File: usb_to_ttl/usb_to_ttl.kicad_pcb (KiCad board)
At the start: 2 copper layers, 15 parts, among them J1 Debug, P1 USB_C_Plug_USB2.0, P2 USB_C_Plug_USB2.0, U1 CP2102N-Axx-xQFN28, U2 TLV1117-33

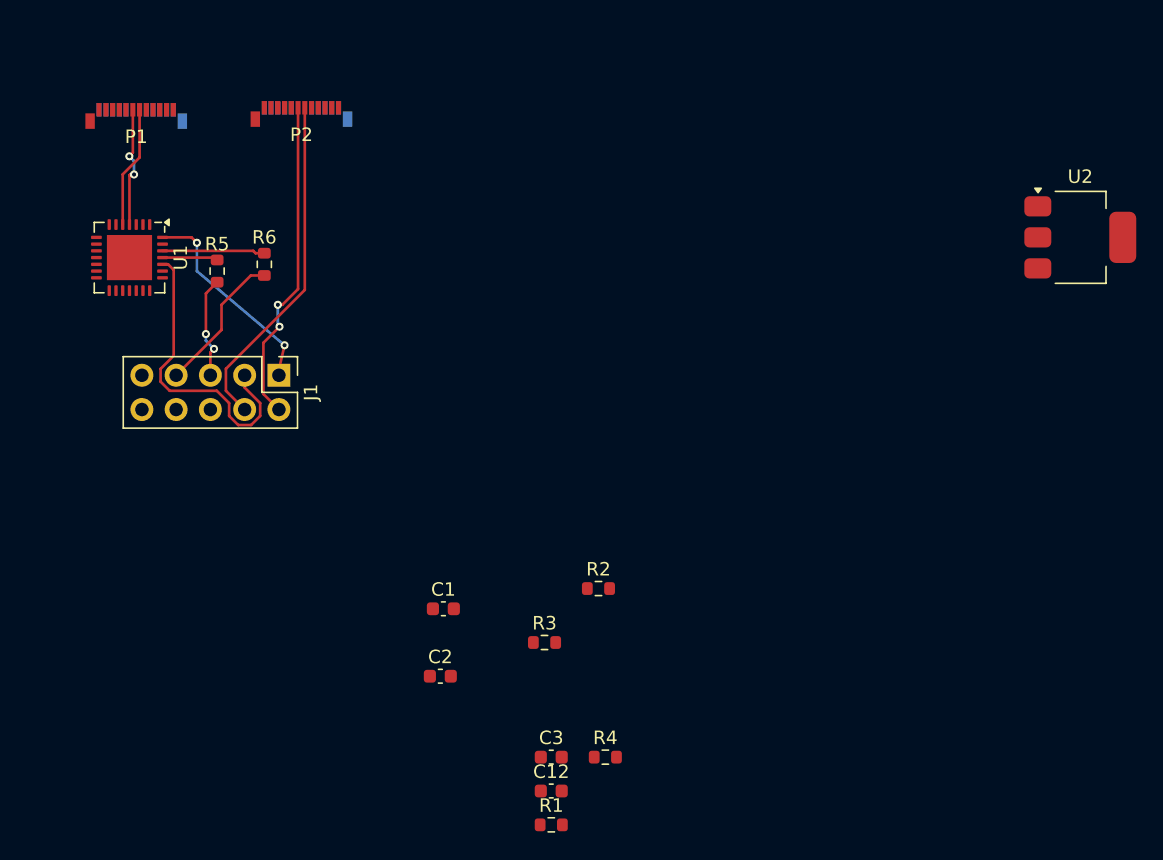
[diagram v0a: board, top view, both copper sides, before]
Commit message: Updated adapter/debugger schematic and PCB files
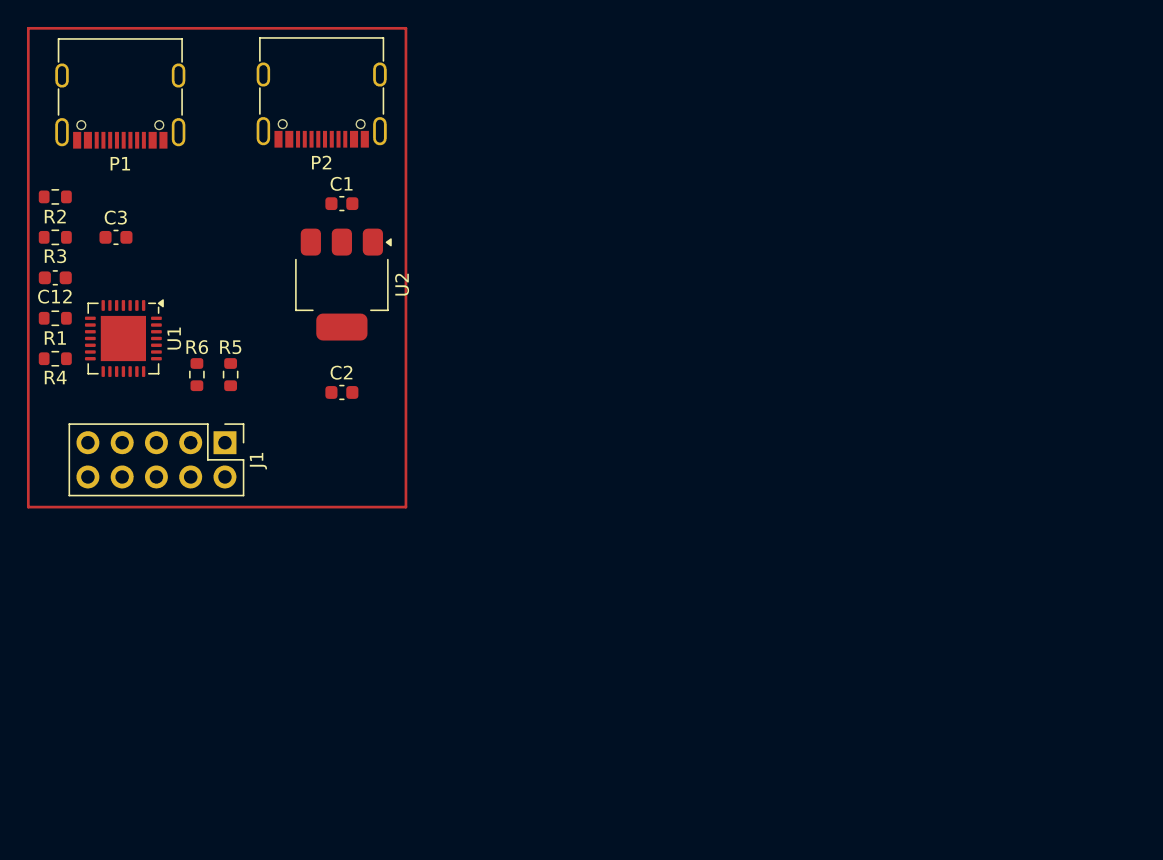
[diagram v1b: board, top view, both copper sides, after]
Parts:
- P1, P2: footprint Connector_USB:USB_C_Plug_Molex_105444 -> Connector_USB:USB_C_Receptacle_G-Switch_GT-USB-7010ASV
- moved U2 54.9 mm to (37.2, 30.0), turned to -90 degrees
- moved C12 52.9 mm to (16.0, 29.5), turned to 180 degrees
- moved R1 52.6 mm to (16.0, 32.5)
- moved R4 50.4 mm to (16.0, 35.5), turned to 180 degrees
- moved C3 50.3 mm to (20.5, 26.5)
- moved R2 49.7 mm to (16.0, 23.5)
- moved R3 47.1 mm to (16.0, 26.5), turned to 180 degrees
- moved C1 31.0 mm to (37.2, 24.0)
- moved C2 22.3 mm to (37.2, 38.0)
- moved R6 9.58 mm to (26.5, 36.7)
- moved R5 7.74 mm to (29.0, 36.7)
- moved J1 6.40 mm to (28.6, 41.7)
- moved U1 6.02 mm to (21.1, 34.0)
- moved P2 2.02 mm to (35.8, 15.5), turned to 180 degrees
- moved P1 1.85 mm to (20.8, 15.6), turned to 180 degrees
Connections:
- J1 pad 2: /USB_D+ -> /USB2_D+
- J1 pad 4: /USB_D- -> /USB2_D-
- P1 pad A6: /USB_D+ -> /USB1_D+
- P1 pad A7: /USB_D- -> /USB1_D-
- P1 pad S1: unconnected-(P1-SHIELD-PadS1)_1 -> GND
- P2 pad A6: /USB_D+ -> /USB2_D+
- P2 pad A7: /USB_D- -> /USB2_D-
- P2 pad S1: unconnected-(P2-SHIELD-PadS1)_1 -> GND
- U1 pad 4: /USB_D+ -> /USB1_D+
- U1 pad 5: /USB_D- -> /USB1_D-
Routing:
- net /USB_D-: track 34.4 -> 0.00 mm
- net /USB_D+: track 33.3 -> 0.00 mm, vias 4 -> 0
- net /RTS: track 22.7 -> 0.00 mm
- net /DTR: track 15.6 -> 0.00 mm, vias 2 -> 0
- net /RX: track 10.7 -> 0.00 mm
- net Net-(U1-TXD): track 7.62 -> 0.00 mm
- net /TX: track 7.60 -> 0.00 mm, vias 2 -> 0
- net Net-(U1-RXD): track 4.12 -> 0.00 mm

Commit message: USB to TTL Adapter design complete
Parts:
- C2: footprint Capacitor_SMD:C_0603_1608Metric -> Capacitor_SMD:C_0805_2012Metric
- moved R1 1.12 mm to (15.5, 33.5)
- moved R4 1.12 mm to (15.5, 36.5)
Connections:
- J1 pad 5: /TX -> /RX
- J1 pad 7: /RX -> /TX
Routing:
- net +3V3: track 0.00 -> 44.7 mm
- net +5V: track 0.00 -> 44.4 mm
- net /USB2_D-: track 0.00 -> 31.8 mm, vias 0 -> 2
- net /USB2_D+: track 0.00 -> 31.6 mm, vias 0 -> 2
- net /DTR: track 0.00 -> 14.7 mm
- net /RTS: track 0.00 -> 14.3 mm
- net /USB1_D+: track 0.00 -> 12.7 mm, vias 0 -> 2
- net /USB1_D-: track 0.00 -> 12.4 mm, vias 0 -> 2
- net Net-(U1-VBUS): track 0.00 -> 10.1 mm, vias 0 -> 2
- net /TX: track 0.00 -> 8.13 mm
- net /RX: track 0.00 -> 7.29 mm
- net GND: track 0.00 -> 6.88 mm, vias 0 -> 5
- net Net-(U1-RXD): track 0.00 -> 6.27 mm
- net Net-(U1-TXD): track 0.00 -> 5.46 mm, vias 0 -> 2
- net Net-(U1-SUSPEND): track 0.00 -> 3.85 mm
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- added copper zone on B.Cu, net GND
- added copper zone on F.Cu, net GND
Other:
- board outline added: 31 x 37.5 mm
- board text added: "${TITLE} ${ISSUE_DATE} ${REVISION} ${COMPANY}"

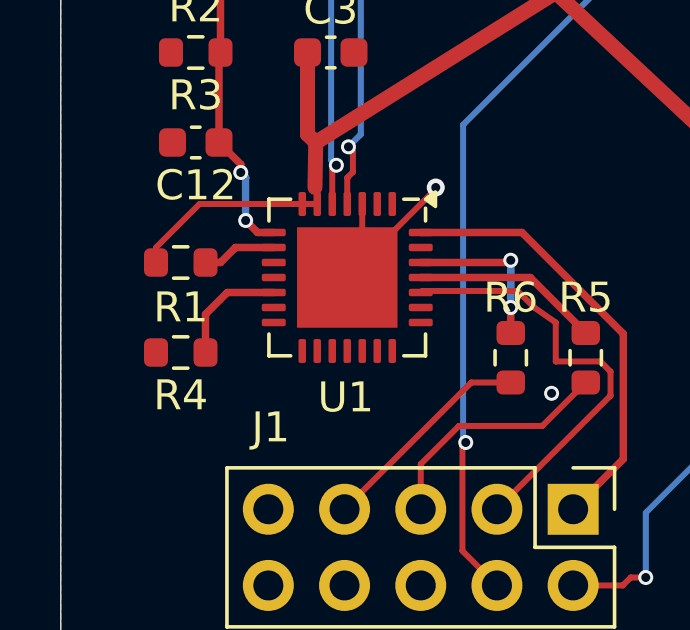
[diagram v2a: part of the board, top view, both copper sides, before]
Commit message: Fixed connection to SUSPEND pins
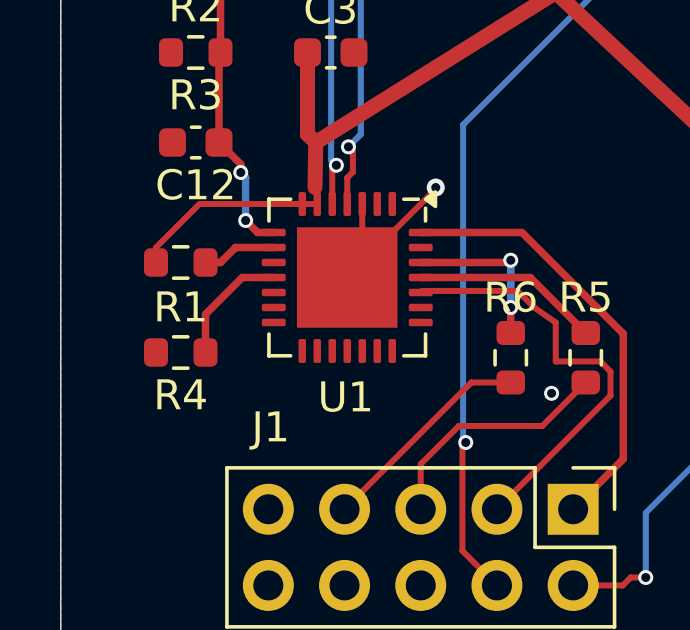
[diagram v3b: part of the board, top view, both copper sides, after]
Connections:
- R4 pad 1: Net-(U1-SUSPEND) -> Net-(U1-~{SUSPEND})
- U1 pad 11: unconnected-(U1-~{SUSPEND}-Pad11) -> Net-(U1-~{SUSPEND})
- U1 pad 12: Net-(U1-SUSPEND) -> unconnected-(U1-SUSPEND-Pad12)
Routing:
- net Net-(U1-~{SUSPEND}): track 0.00 -> 4.06 mm
- net Net-(U1-SUSPEND): track 3.85 -> 0.00 mm
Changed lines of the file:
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@@
 	(net 8 "/RTS")
 	(net 9 "Net-(U1-~{RST})")
-	(net 10 "Net-(U1-SUSPEND)")
+	(net 10 "Net-(U1-~{SUSPEND})")
 	(net 11 "Net-(U1-TXD)")
 	(net 12 "unconnected-(U1-~{RI}{slash}CLK-Pad2)")
-	(net 13 "unconnected-(U1-~{SUSPEND}-Pad11)")
+	(net 13 "unconnected-(U1-SUSPEND-Pad12)")
 	(net 14 "unconnected-(U1-GPIO.5-Pad21)")
 	(net 15 "unconnected-(U1-~{DSR}-Pad27)")
@@
 			(layers "F.Cu" "F.Mask" "F.Paste")
 			(roundrect_rratio 0.25)
-			(net 10 "Net-(U1-SUSPEND)")
+			(net 10 "Net-(U1-~{SUSPEND})")
 			(pintype "passive")
 		)
@@
 			(layers "F.Cu" "F.Mask" "F.Paste")
 			(roundrect_rratio 0.25)
-			(net 13 "unconnected-(U1-~{SUSPEND}-Pad11)")
+			(net 10 "Net-(U1-~{SUSPEND})")
 			(pinfunction "~{SUSPEND}")
-			(pintype "output+no_connect")
+			(pintype "output")
 		)
 		(pad "12" smd roundrect
@@
 			(layers "F.Cu" "F.Mask" "F.Paste")
 			(roundrect_rratio 0.25)
-			(net 10 "Net-(U1-SUSPEND)")
+			(net 13 "unconnected-(U1-SUSPEND-Pad12)")
 			(pinfunction "SUSPEND")
-			(pintype "output")
+			(pintype "output+no_connect")
 		)
 		(pad "13" smd roundrect
@@
 	)
 	(segment
-		(start 18.6 34.5)
-		(end 17.049418 34.5)
+		(start 16.325 36.5)
+		(end 16.325 35.224418)
 		(width 0.25)
 		(layer "F.Cu")
@@
 	)
 	(segment
-		(start 16.325 35.224418)
-		(end 16.325 36.5)
+		(start 17.549418 34)
+		(end 18.6 34)
 		(width 0.25)
 		(layer "F.Cu")
@@
 	)
 	(segment
-		(start 17.049418 34.5)
-		(end 16.325 35.224418)
+		(start 16.325 35.224418)
+		(end 17.549418 34)
 		(width 0.25)
 		(layer "F.Cu")

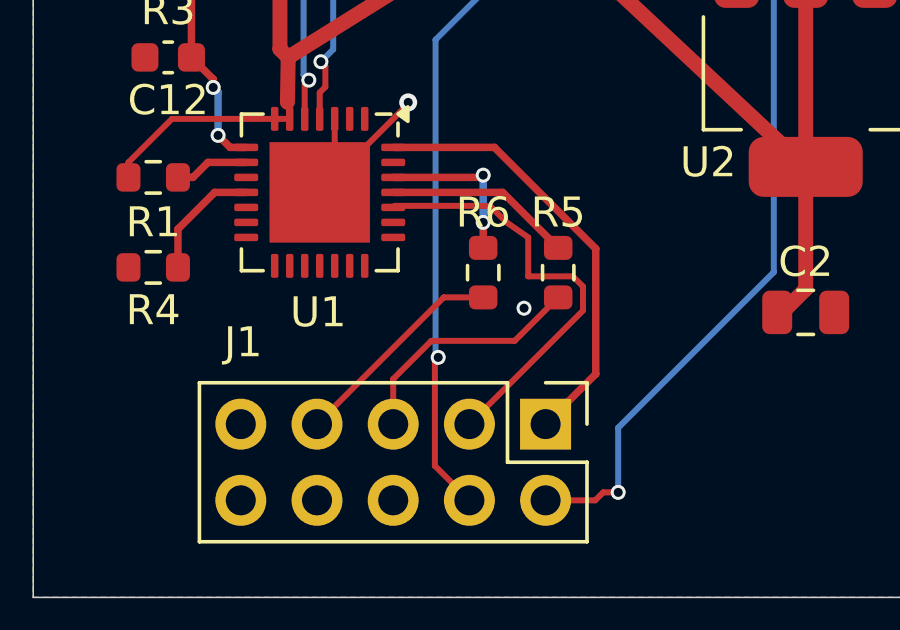
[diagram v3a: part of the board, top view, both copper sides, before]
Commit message: Fixed TX/RX connection on the board
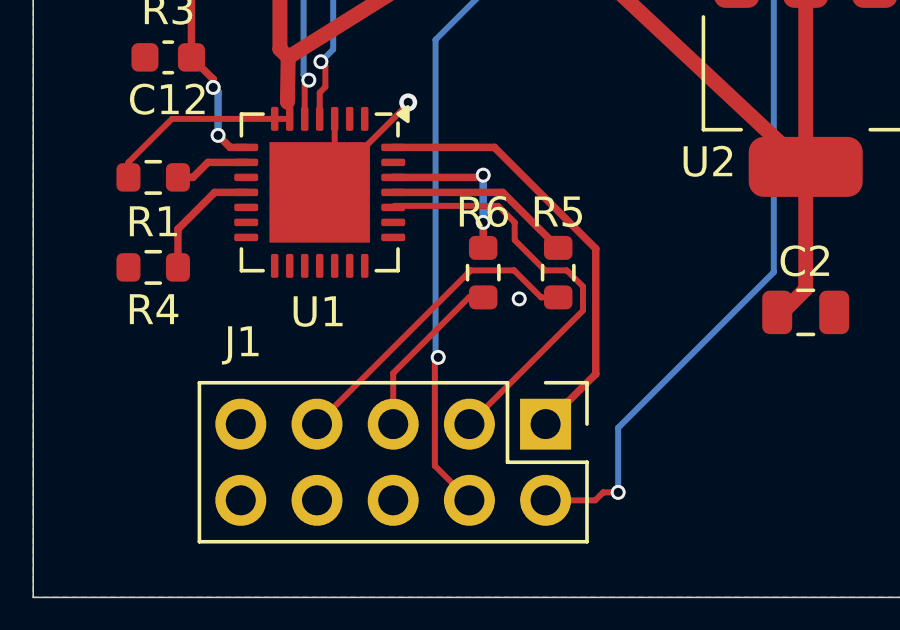
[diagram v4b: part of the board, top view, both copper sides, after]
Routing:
- net /TX: track 8.13 -> 10.5 mm
- net /RX: track 7.29 -> 5.75 mm
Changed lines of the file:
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@@
 	)
 	(via
-		(at 27.861091 37.861091)
+		(at 27.7 37.55)
 		(size 0.5)
 		(drill 0.3)
@@
 	)
 	(segment
-		(start 25.185 37.5)
-		(end 20.96 41.725)
+		(start 26.5 37.5)
+		(end 26.025 37.5)
 		(width 0.2)
 		(layer "F.Cu")
@@
 	)
 	(segment
-		(start 26.5 37.5)
-		(end 25.185 37.5)
+		(start 23.5 40.025)
+		(end 23.5 41.725)
+		(width 0.2)
+		(layer "F.Cu")
+		(net 5)
+	)
+	(segment
+		(start 26.025 37.5)
+		(end 23.5 40.025)
 		(width 0.2)
 		(layer "F.Cu")
@@
 	)
 	(segment
+		(start 26.085 36.6)
+		(end 20.96 41.725)
+		(width 0.2)
+		(layer "F.Cu")
+		(net 7)
+	)
+	(segment
 		(start 29 37.5)
-		(end 27.551 38.949)
+		(end 28.429232 37.5)
 		(width 0.2)
 		(layer "F.Cu")
@@
 	)
 	(segment
-		(start 27.551 38.949)
-		(end 24.771768 38.949)
+		(start 28.429232 37.5)
+		(end 27.529232 36.6)
 		(width 0.2)
 		(layer "F.Cu")
@@
 	)
 	(segment
-		(start 24.771768 38.949)
-		(end 23.5 40.220768)
+		(start 27.529232 36.6)
+		(end 26.085 36.6)
 		(width 0.2)
 		(layer "F.Cu")
 		(net 7)
-	)
-	(segment
-		(start 23.5 40.220768)
-		(end 23.5 41.725)
-		(width 0.2)
-		(layer "F.Cu")
-		(net 7)
-	)
-	(segment
-		(start 28 35.5)
-		(end 28 36.799)
-		(width 0.2)
-		(layer "F.Cu")
-		(net 8)
-	)
-	(segment
-		(start 27.276 34.996768)
-		(end 28 35.5)
-		(width 0.2)
-		(layer "F.Cu")
-		(net 8)
-	)
-	(segment
-		(start 29.488064 36.799)
-		(end 29.826 37.136936)
-		(width 0.2)
-		(layer "F.Cu")
-		(net 8)
 	)
 	(segment
@@
 	)
 	(segment
+		(start 29.289064 36.6)
+		(end 29.826 37.136936)
+		(width 0.2)
+		(layer "F.Cu")
+		(net 8)
+	)
+	(segment
+		(start 28.560936 36.6)
+		(end 29.289064 36.6)
+		(width 0.2)
+		(layer "F.Cu")
+		(net 8)
+	)
+	(segment
 		(start 23.551 34.449)
-		(end 26.728232 34.449)
-		(width 0.2)
-		(layer "F.Cu")
-		(net 8)
-	)
-	(segment
-		(start 26.728232 34.449)
-		(end 27.276 34.996768)
-		(width 0.2)
-		(layer "F.Cu")
-		(net 8)
-	)
-	(segment
-		(start 28 36.799)
-		(end 29.488064 36.799)
+		(end 26.996546 34.449)
+		(width 0.2)
+		(layer "F.Cu")
+		(net 8)
+	)
+	(segment
+		(start 26.996546 34.449)
+		(end 27.55 35.002454)
+		(width 0.2)
+		(layer "F.Cu")
+		(net 8)
+	)
+	(segment
+		(start 27.55 35.002454)
+		(end 27.55 35.589064)
 		(width 0.2)
 		(layer "F.Cu")
@@
 		(width 0.2)
 		(layer "F.Cu")
+		(net 8)
+	)
+	(segment
+		(start 27.55 35.589064)
+		(end 28.560936 36.6)
+		(width 0.2)
+		(layer "F.Cu")

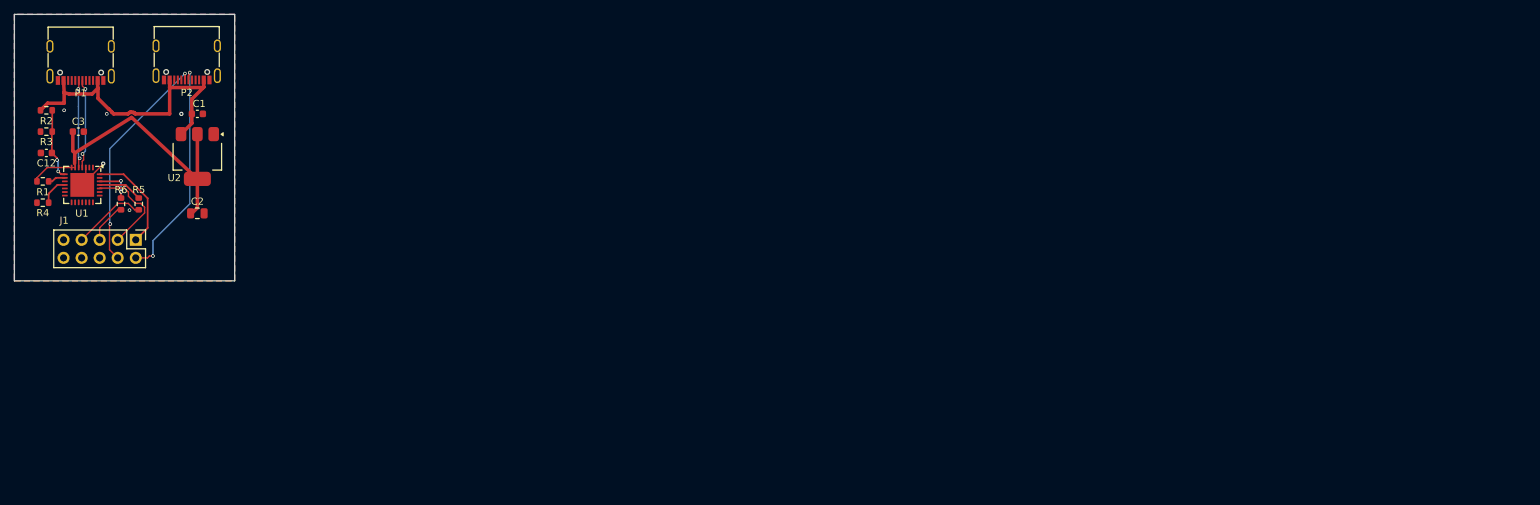
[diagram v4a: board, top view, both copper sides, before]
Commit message: Added mounting holes
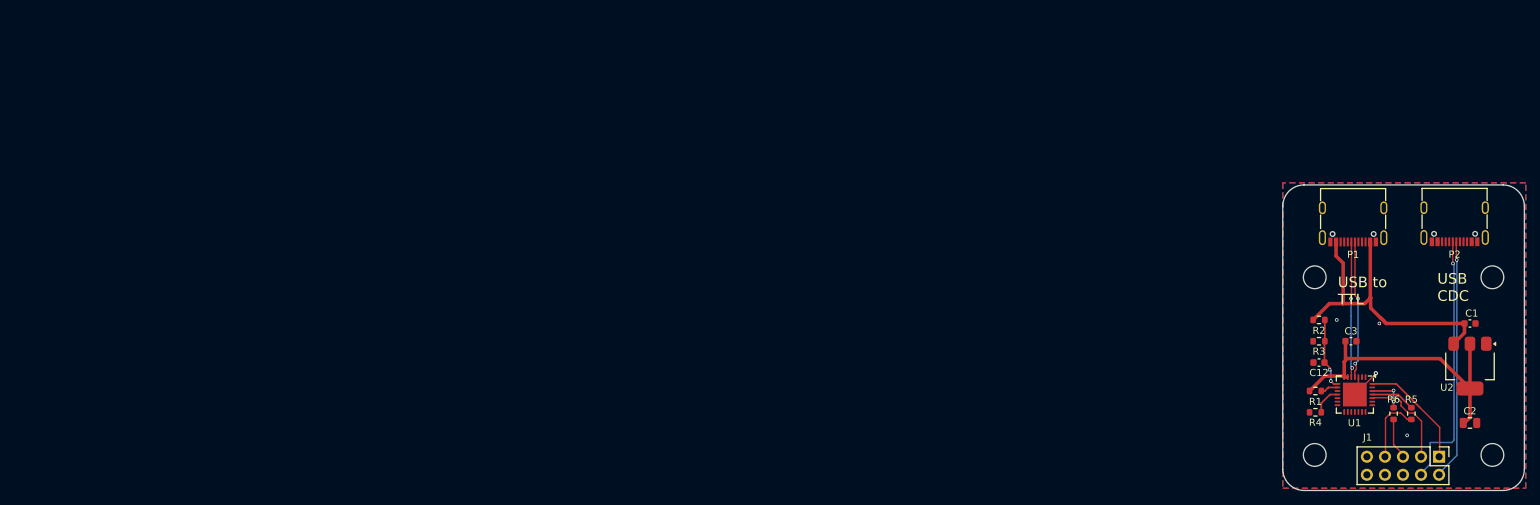
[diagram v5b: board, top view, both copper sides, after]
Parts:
- added H1: MountingHole, MountingHole:MountingHole_3.2mm_M3_ISO7380, F.Cu at (194.5, 47.0)
- added H2: MountingHole, MountingHole:MountingHole_3.2mm_M3_ISO7380, F.Cu at (219.5, 47.0)
- added H3: MountingHole, MountingHole:MountingHole_3.2mm_M3_ISO7380, F.Cu at (194.5, 72.0)
- added H4: MountingHole, MountingHole:MountingHole_3.2mm_M3_ISO7380, F.Cu at (219.5, 72.0)
- moved J1 185.9 mm to (212.0, 72.2)
- moved C1 181.5 mm to (216.3, 53.5)
- moved C12 181.5 mm to (195.1, 59.0)
- moved C2 181.5 mm to (216.3, 67.5)
- moved C3 181.5 mm to (199.6, 56.0)
- moved R1 181.5 mm to (194.6, 63.0)
- moved R2 181.5 mm to (195.1, 53.0)
- moved R3 181.5 mm to (195.1, 56.0)
- moved R4 181.5 mm to (194.6, 66.0)
- moved R5 181.5 mm to (208.1, 66.2)
- moved R6 181.5 mm to (205.6, 66.2)
- moved U2 181.5 mm to (216.3, 59.5)
- moved U1 181.5 mm to (200.1, 63.5)
- moved P1 180.5 mm to (199.9, 38.3)
- moved P2 179.9 mm to (214.2, 38.3)
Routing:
- net /USB1_D+: track 12.7 -> 19.5 mm
- net /USB1_D-: track 12.4 -> 19.2 mm
- net /USB2_D-: track 31.8 -> 36.6 mm, vias 2 -> 1
- net +3V3: track 44.7 -> 41.8 mm
- net /USB2_D+: track 31.6 -> 33.9 mm, vias 2 -> 1
- net /DTR: track 14.7 -> 16.2 mm
- net +5V: track 44.4 -> 45.5 mm
- net /TX: track 10.5 -> 9.77 mm
- net GND: vias 5 -> 4
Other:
- board size 31 x 37.5 mm -> 34 x 43 mm
- board text added: "Mounting Holes are 25x25mm"
- board text added: "USB CDC"
- board text added: "USB to TTL"
